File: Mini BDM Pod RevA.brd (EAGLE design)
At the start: 50 x 27 mm, 37 parts

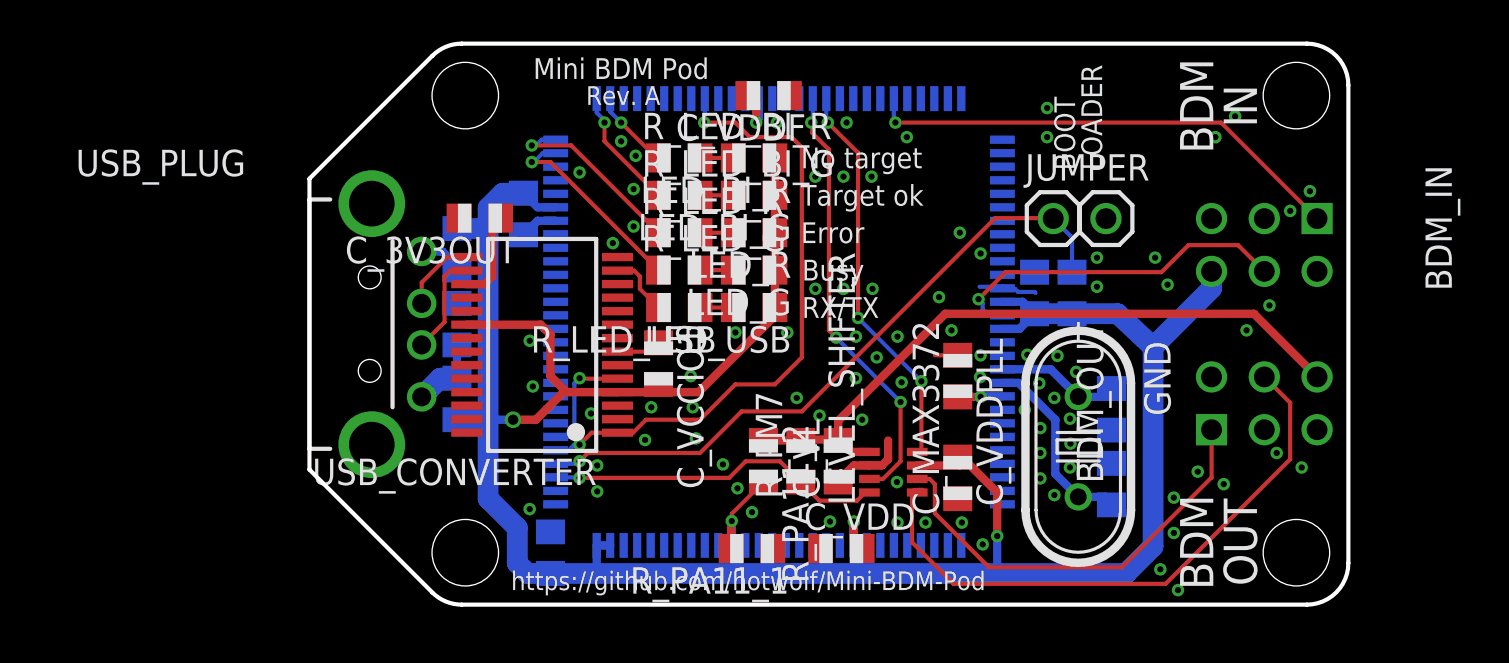
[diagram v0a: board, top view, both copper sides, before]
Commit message: prepared mounting diagram
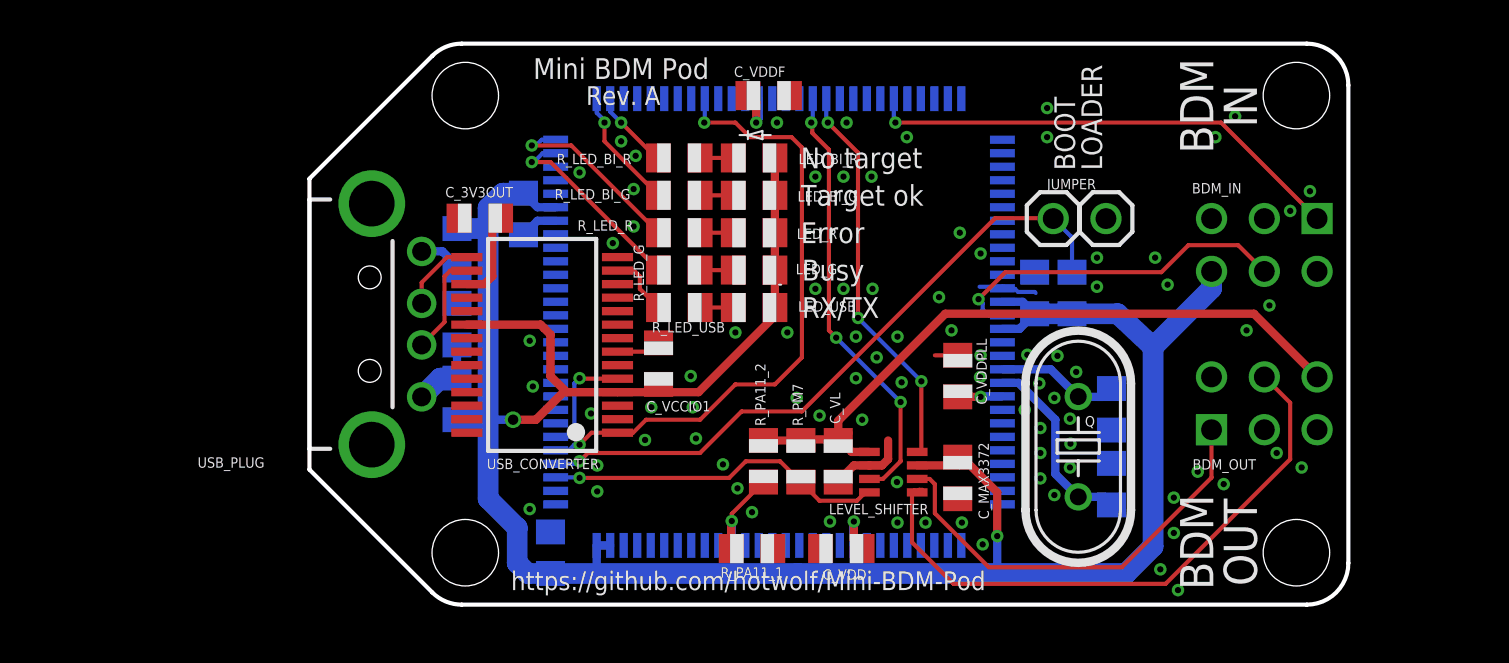
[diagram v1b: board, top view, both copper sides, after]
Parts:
- renumbered GND to Q
